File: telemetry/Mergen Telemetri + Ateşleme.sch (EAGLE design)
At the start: 78 parts, among them J2 U.FL, Q2 IRLML6344TRPBF, Q3 IRLML6344TRPBF, U1 STM32F401CCU6UFQFPN-48_7X7X0P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, U2 ADXL345BCCZ, U3 LPS22HB, U4 L86, U6 AMS1117-3.3, U7 AMS1117-3.3, Y1 ABM3B-26.000MHZ-10-1-U-T

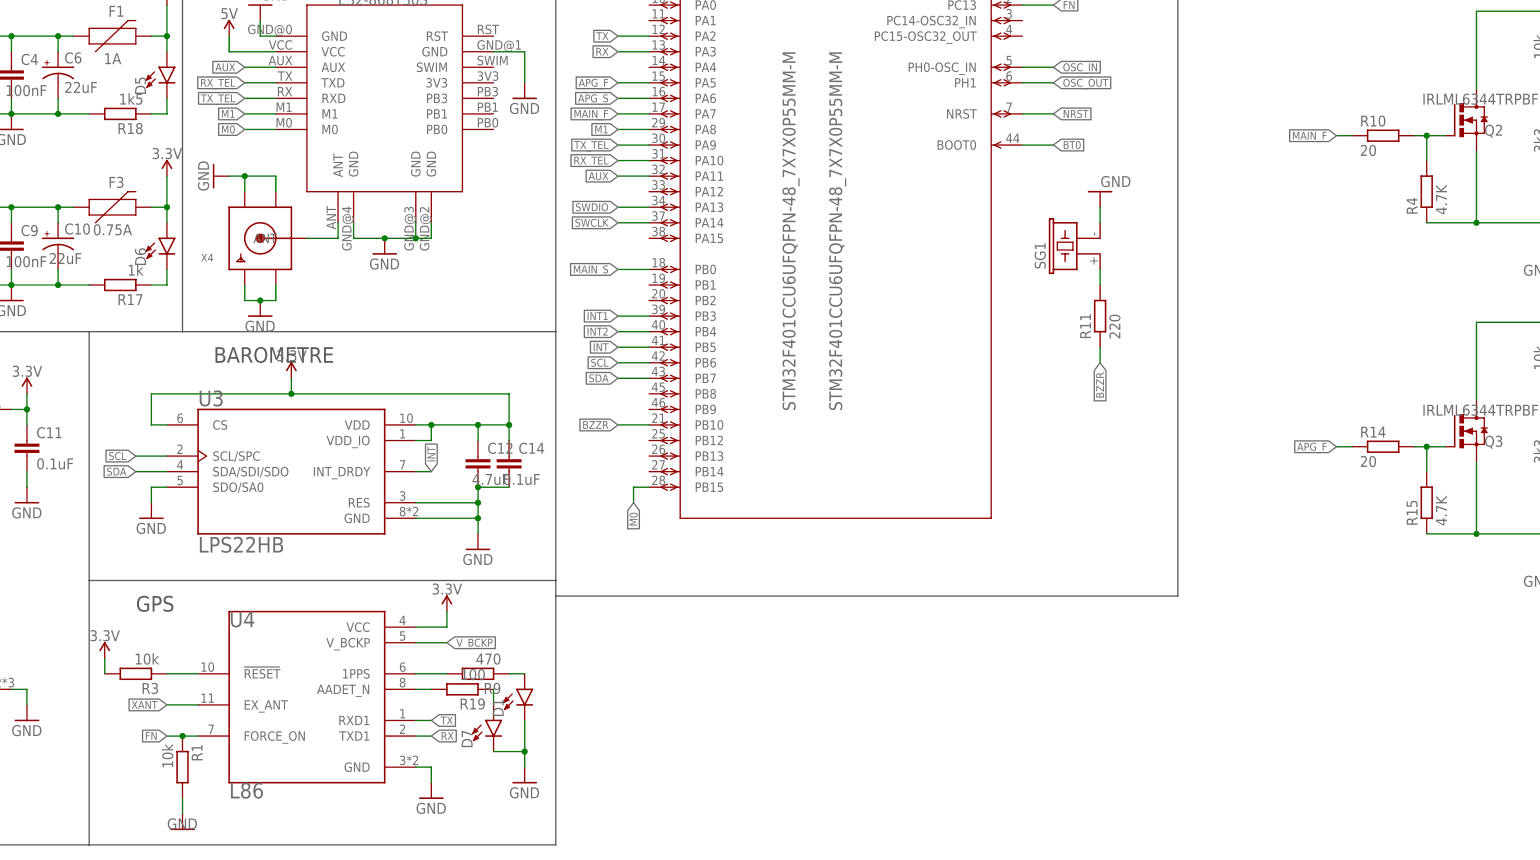
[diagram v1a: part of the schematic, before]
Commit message: Routes were be extended
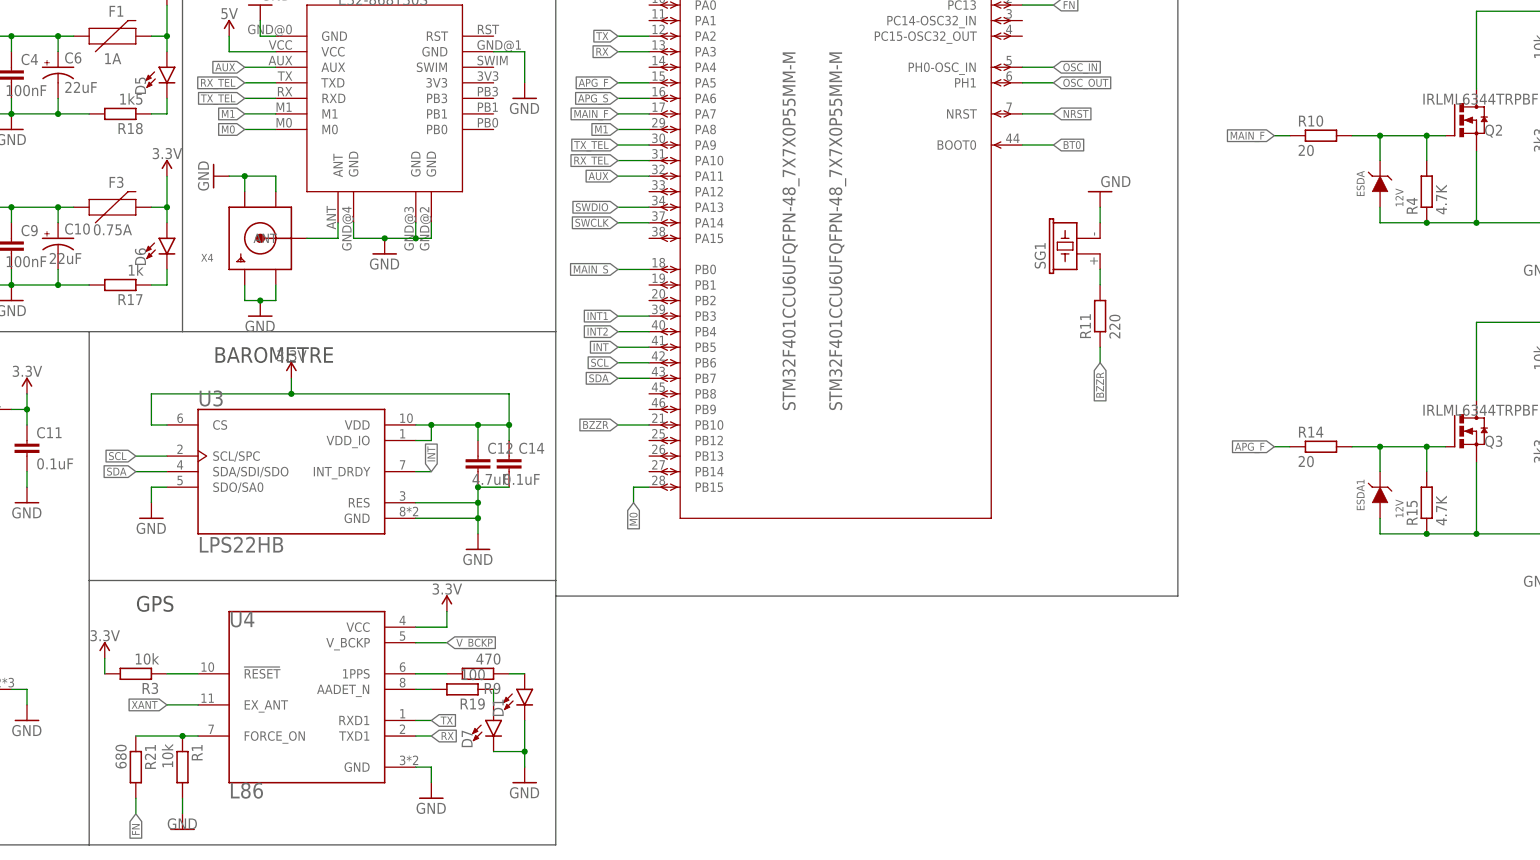
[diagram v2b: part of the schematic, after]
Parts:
- added ESDA, ESDA1: 12V, Wurth_EMC Components_WE-TVSP:WE-TVSP_DO-214AC_400W_UNI_824500102
- added R21: 680, rcl:R-EU_R0402
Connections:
- new net N$20: R1.1, R21.1, U4.FORCE_ON
- net FN: now also R21.2; no longer R1.1, U4.FORCE_ON
- net GND: now also ESDA.A, ESDA1.A
- net N$13: now also ESDA.C
- net N$6: now also ESDA1.C
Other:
- moved on the sheet: R10, R14
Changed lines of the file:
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@@
 <part name="C25" library="rcl" library_urn="urn:adsk.eagle:library:334" deviceset="C-EU" device="C0402K" package3d_urn="urn:adsk.eagle:package:23679/2" value="0.1uF"/>
 <part name="C28" library="rcl" library_urn="urn:adsk.eagle:library:334" deviceset="C-EU" device="C0402K" package3d_urn="urn:adsk.eagle:package:23679/2" value="0.1uF"/>
+<part name="ESDA" library="Wurth_EMC Components_WE-TVSP" library_urn="urn:adsk.eagle:library:14283044" deviceset="WE-TVSP_DO-214AC_400W_UNI" device="" package3d_urn="urn:adsk.eagle:package:12146528/2" technology="_824500102" value="12V"/>
+<part name="ESDA1" library="Wurth_EMC Components_WE-TVSP" library_urn="urn:adsk.eagle:library:14283044" deviceset="WE-TVSP_DO-214AC_400W_UNI" device="" package3d_urn="urn:adsk.eagle:package:12146528/2" technology="_824500102" value="12V"/>
+<part name="R21" library="rcl" library_urn="urn:adsk.eagle:library:334" deviceset="R-EU_" device="R0402" package3d_urn="urn:adsk.eagle:package:23547/3" value="680"/>
 </parts>
 <sheets>
@@
 <attribute name="VALUE" x="147.828" y="-1.016" size="1.778" layer="96"/>
 </instance>
-<instance part="R10" gate="G$1" x="124.968" y="21.844" smashed="yes">
-<attribute name="NAME" x="121.158" y="23.3426" size="1.778" layer="95"/>
-<attribute name="VALUE" x="121.158" y="18.542" size="1.778" layer="96"/>
+<instance part="R10" gate="G$1" x="114.808" y="21.844" smashed="yes">
+<attribute name="NAME" x="110.998" y="23.3426" size="1.778" layer="95"/>
+<attribute name="VALUE" x="110.998" y="18.542" size="1.778" layer="96"/>
 </instance>
 <instance part="P+17" gate="VCC" x="-91.44" y="78.74" smashed="yes">
@@
 <attribute name="VALUE" x="147.828" y="-51.816" size="1.778" layer="96"/>
 </instance>
-<instance part="R14" gate="G$1" x="124.968" y="-28.956" smashed="yes">
-<attribute name="NAME" x="121.158" y="-27.4574" size="1.778" layer="95"/>
-<attribute name="VALUE" x="121.158" y="-32.258" size="1.778" layer="96"/>
+<instance part="R14" gate="G$1" x="114.808" y="-28.956" smashed="yes">
+<attribute name="NAME" x="110.998" y="-27.4574" size="1.778" layer="95"/>
+<attribute name="VALUE" x="110.998" y="-32.258" size="1.778" layer="96"/>
 </instance>
 <instance part="R15" gate="G$1" x="132.08" y="-38.1" smashed="yes" rot="R90">
@@
 <attribute name="NAME" x="82.804" y="114.681" size="1.778" layer="95"/>
 <attribute name="VALUE" x="80.264" y="109.601" size="1.778" layer="96"/>
+</instance>
+<instance part="ESDA" gate="G$1" x="124.46" y="15.24" smashed="yes" rot="R90">
+<attribute name="NAME" x="121.92" y="13.97" size="1.27" layer="95" rot="R90" align="bottom-center"/>
+<attribute name="VALUE" x="128.27" y="10.16" size="1.27" layer="96" rot="R90"/>
+</instance>
+<instance part="ESDA1" gate="G$1" x="124.46" y="-35.56" smashed="yes" rot="R90">
+<attribute name="NAME" x="121.92" y="-36.83" size="1.27" layer="95" rot="R90" align="bottom-center"/>
+<attribute name="VALUE" x="128.27" y="-40.64" size="1.27" layer="96" rot="R90"/>
+</instance>
+<instance part="R21" gate="G$1" x="-78.74" y="-81.28" smashed="yes" rot="R270">
+<attribute name="NAME" x="-77.2414" y="-77.47" size="1.778" layer="95" rot="R270"/>
+<attribute name="VALUE" x="-82.042" y="-77.47" size="1.778" layer="96" rot="R270"/>
 </instance>
 </instances>
@@
 <wire x1="140.208" y1="19.304" x2="140.208" y2="7.62" width="0.1524" layer="91"/>
 <junction x="140.208" y="7.62"/>
+<pinref part="ESDA" gate="G$1" pin="A"/>
+<wire x1="124.46" y1="10.16" x2="124.46" y2="7.62" width="0.1524" layer="91"/>
+<wire x1="124.46" y1="7.62" x2="132.08" y2="7.62" width="0.1524" layer="91"/>
+<junction x="132.08" y="7.62"/>
 </segment>
 <segment>
@@
 <wire x1="140.208" y1="-31.496" x2="140.208" y2="-43.18" width="0.1524" layer="91"/>
 <junction x="140.208" y="-43.18"/>
+<pinref part="ESDA1" gate="G$1" pin="A"/>
+<wire x1="124.46" y1="-40.64" x2="124.46" y2="-43.18" width="0.1524" layer="91"/>
+<wire x1="124.46" y1="-43.18" x2="132.08" y2="-43.18" width="0.1524" layer="91"/>
+<junction x="132.08" y="-43.18"/>
 </segment>
 <segment>
@@
 <net name="FN" class="0">
 <segment>
-<pinref part="U4" gate="G$1" pin="FORCE_ON"/>
-<pinref part="R1" gate="G$1" pin="1"/>
-<wire x1="-68.58" y1="-76.2" x2="-71.12" y2="-76.2" width="0.1524" layer="91"/>
-<wire x1="-71.12" y1="-76.2" x2="-73.66" y2="-76.2" width="0.1524" layer="91"/>
-<junction x="-71.12" y="-76.2"/>
-<label x="-73.66" y="-76.2" size="1.27" layer="95" rot="R180" xref="yes"/>
-</segment>
-<segment>
 <pinref part="U1" gate="A" pin="PC13"/>
 <wire x1="66.04" y1="43.18" x2="71.12" y2="43.18" width="0.1524" layer="91"/>
 <label x="71.12" y="43.18" size="1.27" layer="95" xref="yes"/>
+</segment>
+<segment>
+<pinref part="R21" gate="G$1" pin="2"/>
+<wire x1="-78.74" y1="-86.36" x2="-78.74" y2="-88.9" width="0.1524" layer="91"/>
+<label x="-78.74" y="-88.9" size="1.27" layer="95" rot="R270" xref="yes"/>
 </segment>
 </net>
@@
 <pinref part="R10" gate="G$1" pin="2"/>
 <pinref part="R4" gate="G$1" pin="2"/>
-<wire x1="132.08" y1="21.844" x2="130.048" y2="21.844" width="0.1524" layer="91"/>
+<wire x1="132.08" y1="21.844" x2="124.46" y2="21.844" width="0.1524" layer="91"/>
+<wire x1="124.46" y1="21.844" x2="119.888" y2="21.844" width="0.1524" layer="91"/>
 <wire x1="132.08" y1="17.78" x2="132.08" y2="21.844" width="0.1524" layer="91"/>
 <junction x="132.08" y="21.844"/>
+<pinref part="ESDA" gate="G$1" pin="C"/>
+<wire x1="124.46" y1="17.78" x2="124.46" y2="21.844" width="0.1524" layer="91"/>
+<junction x="124.46" y="21.844"/>
 </segment>
 </net>
@@
 <segment>
 <pinref part="R10" gate="G$1" pin="1"/>
-<wire x1="119.888" y1="21.844" x2="117.348" y2="21.844" width="0.1524" layer="91"/>
-<label x="117.348" y="21.844" size="1.27" layer="95" rot="R180" xref="yes"/>
+<wire x1="109.728" y1="21.844" x2="107.188" y2="21.844" width="0.1524" layer="91"/>
+<label x="107.188" y="21.844" size="1.27" layer="95" rot="R180" xref="yes"/>
 </segment>
 <segment>
@@
 <segment>
 <pinref part="R14" gate="G$1" pin="1"/>
-<wire x1="119.888" y1="-28.956" x2="117.348" y2="-28.956" width="0.1524" layer="91"/>
-<label x="117.348" y="-28.956" size="1.27" layer="95" rot="R180" xref="yes"/>
+<wire x1="109.728" y1="-28.956" x2="107.188" y2="-28.956" width="0.1524" layer="91"/>
+<label x="107.188" y="-28.956" size="1.27" layer="95" rot="R180" xref="yes"/>
 </segment>
 <segment>
@@
 <pinref part="R14" gate="G$1" pin="2"/>
 <pinref part="R15" gate="G$1" pin="2"/>
-<wire x1="132.08" y1="-28.956" x2="130.048" y2="-28.956" width="0.1524" layer="91"/>
+<wire x1="132.08" y1="-28.956" x2="124.46" y2="-28.956" width="0.1524" layer="91"/>
+<wire x1="124.46" y1="-28.956" x2="119.888" y2="-28.956" width="0.1524" layer="91"/>
 <wire x1="132.08" y1="-33.02" x2="132.08" y2="-28.956" width="0.1524" layer="91"/>
 <junction x="132.08" y="-28.956"/>
+<pinref part="ESDA1" gate="G$1" pin="C"/>
+<wire x1="124.46" y1="-33.02" x2="124.46" y2="-28.956" width="0.1524" layer="91"/>
+<junction x="124.46" y="-28.956"/>
 </segment>
 </net>
@@
 </segment>
 </net>
+<net name="N$20" class="0">
+<segment>
+<pinref part="R21" gate="G$1" pin="1"/>
+<pinref part="R1" gate="G$1" pin="1"/>
+<wire x1="-78.74" y1="-76.2" x2="-71.12" y2="-76.2" width="0.1524" layer="91"/>
+<pinref part="U4" gate="G$1" pin="FORCE_ON"/>
+<wire x1="-71.12" y1="-76.2" x2="-68.58" y2="-76.2" width="0.1524" layer="91"/>
+<junction x="-71.12" y="-76.2"/>
+</segment>
+</net>
